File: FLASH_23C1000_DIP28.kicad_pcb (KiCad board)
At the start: 2 copper layers, 16.5 x 34.3 mm, 9 parts, among them J1 uPD23C1000, J2 Conn_1x2, J3 Conn_1x3, U1 29F010 TSOP-32 20mm, U2 29F010 sTSOP-32 14mm, U3 29F010 PLCC-32 7x9

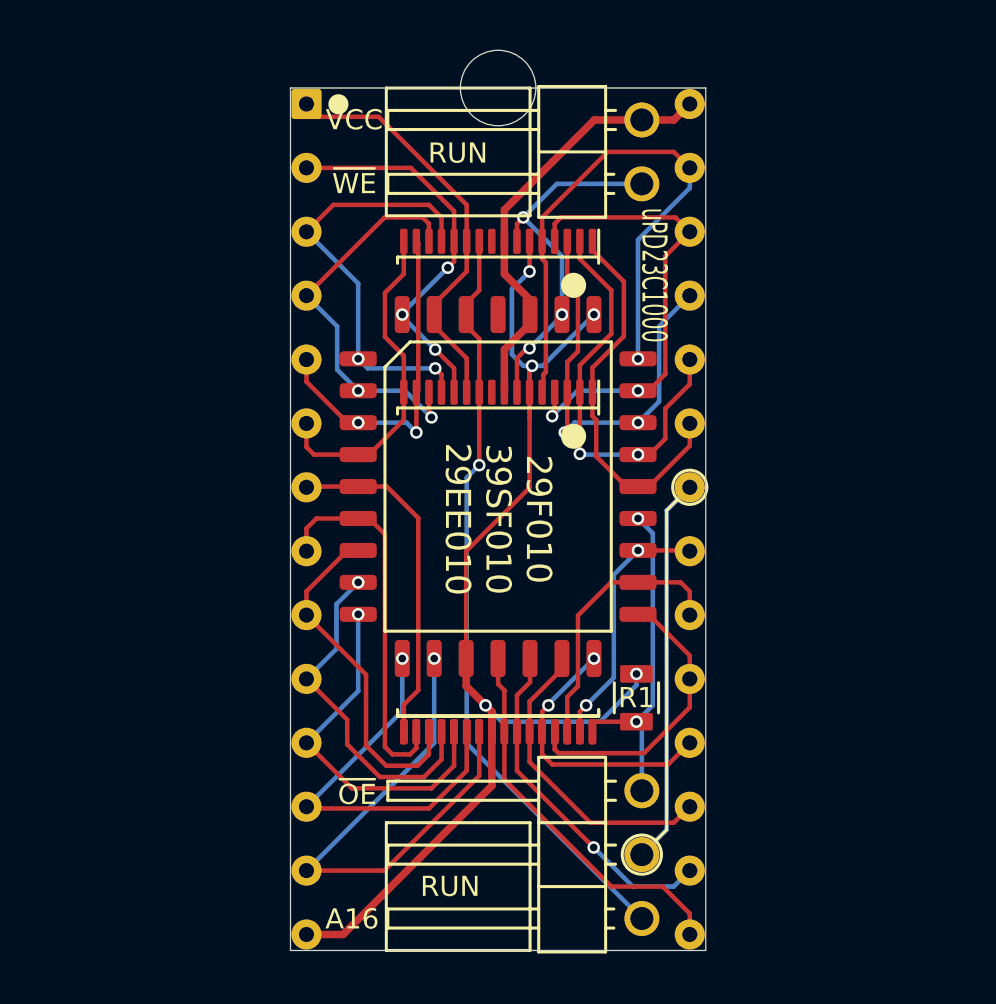
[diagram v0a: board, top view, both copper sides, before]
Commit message: Rename FlashROM_8300 to FLASH_23C1000
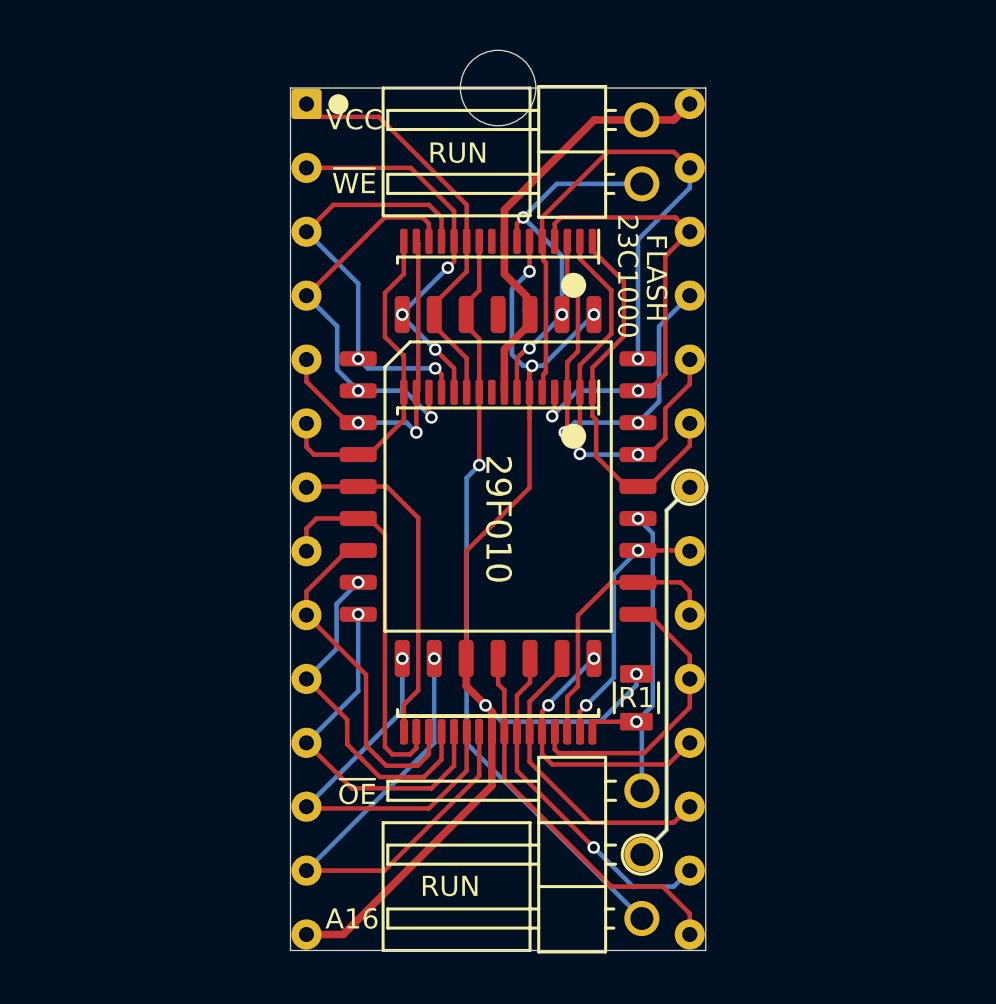
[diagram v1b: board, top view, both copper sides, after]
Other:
- board text added: "23C1000"
- board text added: "29F010"
- board text added: "29F010 to 23C1000"
- board text added: "FLASH"
- board text removed: "29F010 39SF010 29EE010"
- board text removed: "29F010 to uPD23C1000"
- board text removed: "Set programmer for installed chip (ex: SST39SF010 not uPD23C1000)"
- board text removed: "uPD23C1000"

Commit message: kicad 6
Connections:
- net /~CE renamed /~{CE}
- net /~OE renamed /~{OE}
- net /~WE renamed /~{WE}
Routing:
- net /~{CE}: track 10.9 -> 9.97 mm
- net /A17: track 11.8 -> 11.0 mm
- net /A5: track 13.7 -> 13.1 mm
- net /A4: track 13.2 -> 12.7 mm
- net /A2: track 15.0 -> 14.5 mm
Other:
- net class Default removed
- board text added: "Connect ~{WE} to programmer pin 31"
- board text added: "Move the A16 jumper to ~{OE}"
- board text added: "Remove the VCC/~{WE} jumper"
- board text added: "~{OE}"
- board text added: "~{WE}"
- board text removed: "Connect ~WE~ to programmer pin 31"
- board text removed: "Move the A16 jumper to ~OE~"
- board text removed: "Remove the VCC/~WE~ jumper"
- board text removed: "~OE"
- board text removed: "~WE"

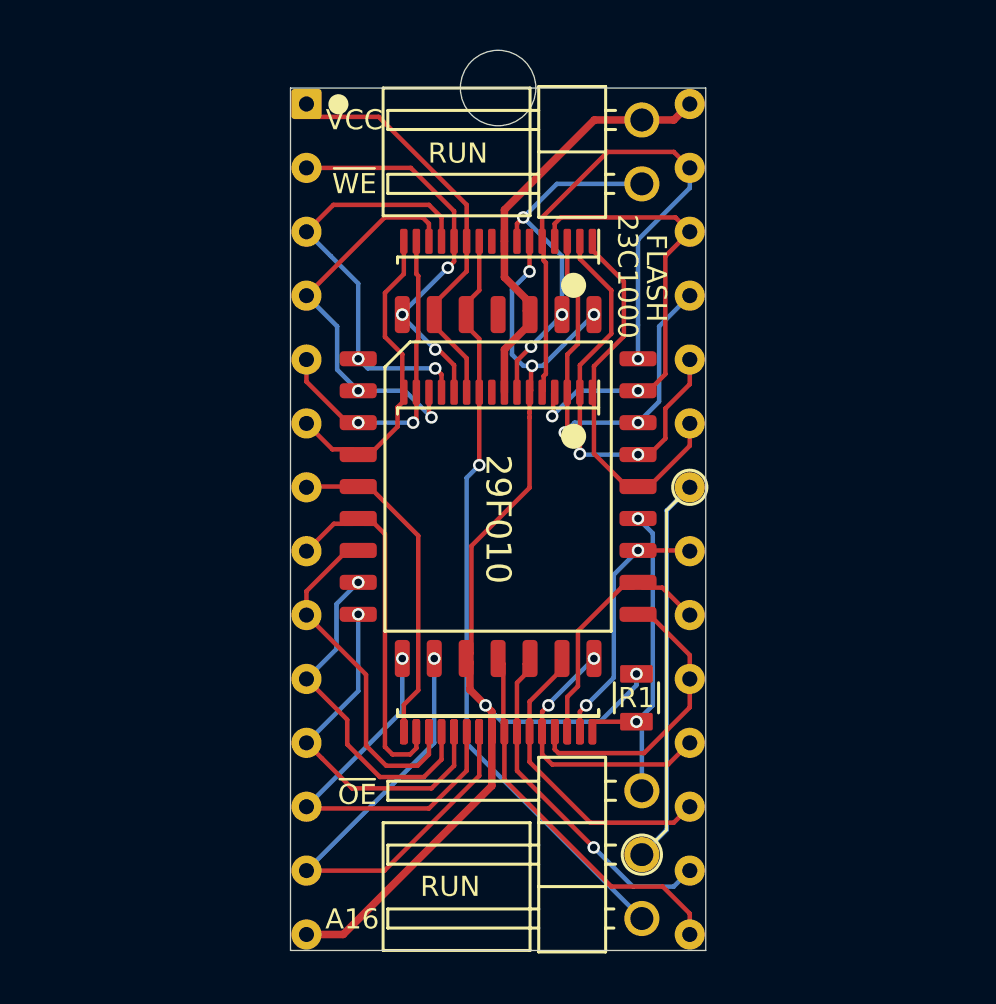
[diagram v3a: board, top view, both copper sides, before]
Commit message: Fix wrong pinout on FlashROM_100 TSOPgit add -A!
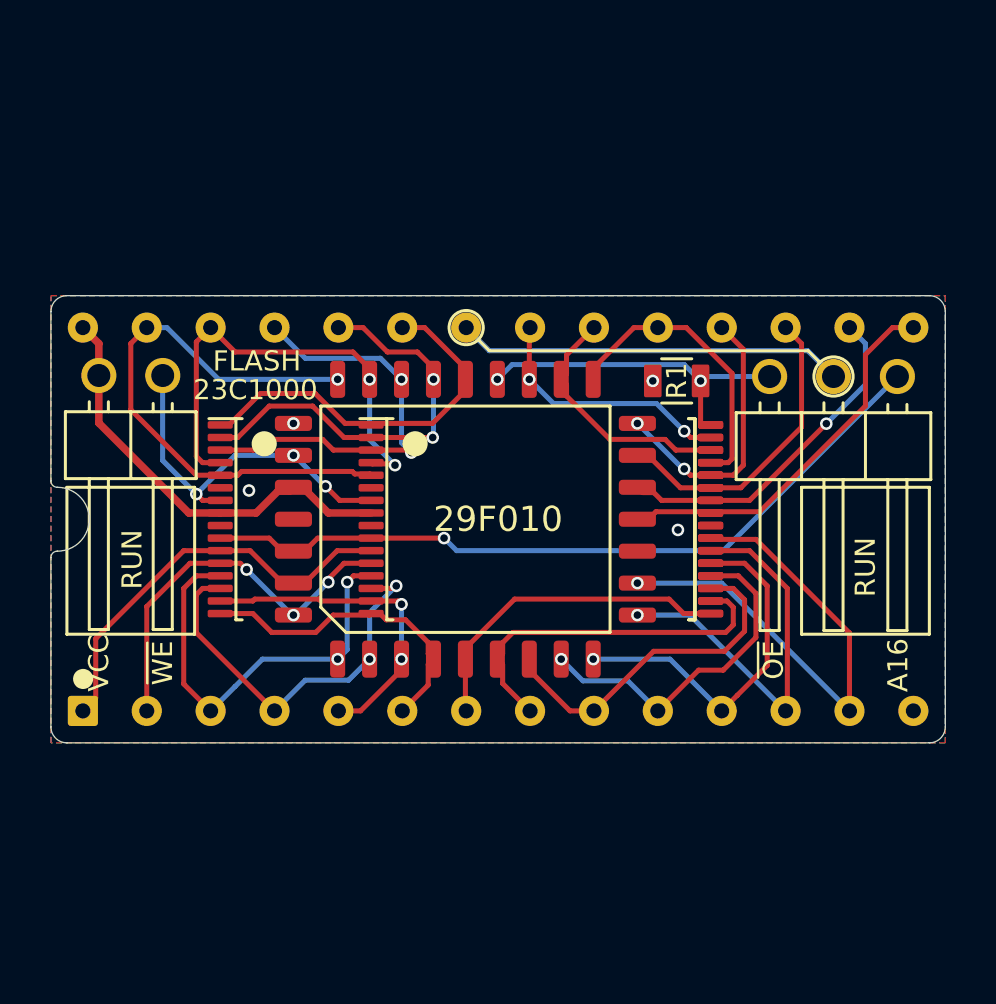
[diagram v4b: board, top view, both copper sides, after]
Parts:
- removed NT1: Net-Tie_2, 000_LOCAL:NetTie-2_SMD_0.18mm
- removed REF**: NPTH_3mm, 000_LOCAL:NPTH_3mm
- J1: value uPD23C1000 -> 23C1000
- moved J3 23.8 mm to (165.9, 93.1), turned to -90 degrees
- moved J2 20.5 mm to (136.7, 93.0), turned to -90 degrees
- moved R1 12.7 mm to (157.1, 93.2), turned to 180 degrees
- moved U2 2.40 mm to (151.7, 98.8), turned to -90 degrees
- moved U1 1.84 mm to (148.7, 98.8), turned to -90 degrees
- moved U3 1.84 mm to (148.7, 98.8), turned to 90 degrees
- turned J1 to 90 degrees
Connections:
- U1 pad 6: /A17 -> /GND
- U1 pad 9: (no net) -> unconnected-(U1-Pad9)
- U2 pad 6: /A17 -> /GND
- U2 pad 9: (no net) -> unconnected-(U2-Pad9)
- U3 pad 1: (no net) -> unconnected-(U3-Pad1)
- U3 pad 30: /A17 -> /GND
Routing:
- net /GND: track 33.3 -> 0.00 mm, vias 2 -> 4
- net /A17: track 11.0 -> 0.00 mm, vias 3 -> 0
- added copper zone on B.Cu, net /GND
- added copper zone on F.Cu, net /GND
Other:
- board size 16.5 x 34.3 mm -> 35.6 x 17.8 mm
- board text added: "${COMMENT1} ${TITLE} ${REVISION}"
- board text added: "R1: ${00000000-0000-0000-0000-00005e638d11:VALUE} Legs: TE 1544210"
- board text added: "To program: Place board in programmer, 2 rows from the top Move the A16 jumper to ~{OE} Connect A16 to programmer pin 2 Remove the VCC/~{WE} jumper Connect ~{WE} to programmer pin 31 Connect VCC to programmer pin 32"
- board text removed: "Connect A16 to programmer pin 2"
- board text removed: "Connect VCC to programmer pin 32"
- board text removed: "Connect ~{WE} to programmer pin 31"
- board text removed: "Legs: TE 1544210"
- board text removed: "Move the A16 jumper to ~{OE}"
- board text removed: "Place board in programmer, 2 rows from the top"
- board text removed: "R1: 47k"
- board text removed: "Remove the VCC/~{WE} jumper"
- board text removed: "To program the flash chip:"
- board text removed: "github.com/bkw777/aDIPters"

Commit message: 23C100 DIP28 outline, gnd, silk
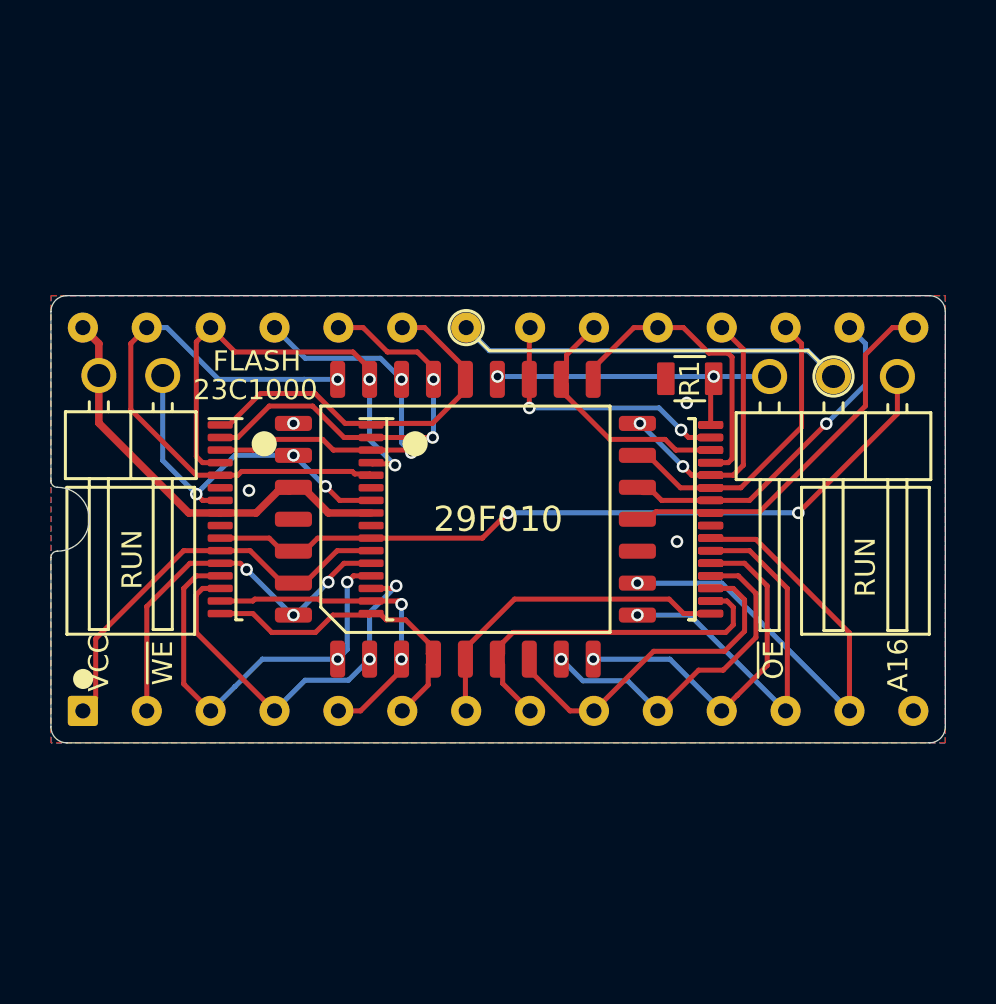
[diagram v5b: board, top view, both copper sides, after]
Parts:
- moved R1 0.53 mm to (157.6, 93.2)
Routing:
- net /~{OE}: track 13.5 -> 12.8 mm
- net /A10: track 10.2 -> 10.9 mm
- net /A16: track 30.4 -> 30.9 mm, vias 1 -> 2
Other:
- board text added: "RUN: Jumper labeled RUN positions. Install board in place of 23C1000. PROGRAM: Place board in programmer, board pin 1 in programmer pin 3. Remove VCC/~{WE} jumper. Move A16 jumper to ~{OE}. Connect A16 to programmer pin 2, ~{WE} to programmer pin 31, VCC to programmer pin 32. Program as 29F010."
- board text removed: "To program: Place board in programmer, 2 rows from the top Move the A16 jumper to ~{OE} Connect A16 to programmer pin 2 Remove the VCC/~{WE} jumper Connect ~{WE} to programmer pin 31 Connect VCC to programmer pin 32"

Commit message: dual tsop footprint on flash_23c100_dip28
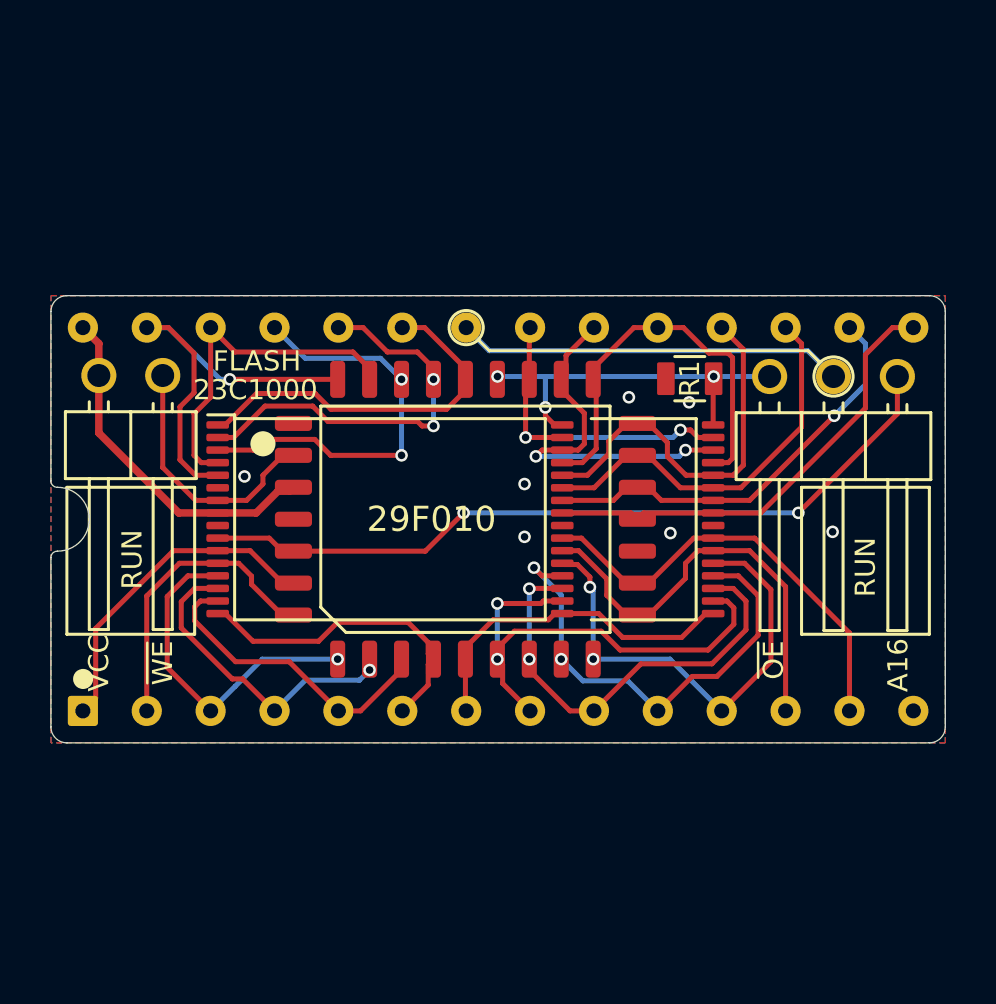
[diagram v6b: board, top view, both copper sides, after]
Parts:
- removed the U2 at (151.7, 98.8)
- U1: value 29F010 TSOP-32 20mm -> 29F010 TSOP-32; footprint 000_LOCAL:TSOP32-20mm -> 000_LOCAL:TSOP32-dual
- turned U1 to 0 degrees
- renumbered U3 to U2
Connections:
- net /GND renamed GND
- net /VCC renamed VCC
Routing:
- net /A14: track 22.7 -> 17.0 mm
- net /A2: track 14.5 -> 19.9 mm, vias 0 -> 2
- net /A0: track 13.6 -> 19.0 mm, vias 1 -> 2
- net /~{CE}: track 9.97 -> 14.8 mm, vias 0 -> 2
- net /A13: track 18.7 -> 13.8 mm, vias 2 -> 0
- net /D0: track 14.3 -> 19.0 mm, vias 1 -> 2
- net /D6: track 11.1 -> 15.6 mm, vias 2 -> 0
- net /D7: track 12.1 -> 16.4 mm
- net /~{WE}: track 14.7 -> 10.3 mm, vias 3 -> 0
- net /A1: track 13.8 -> 17.8 mm, vias 0 -> 2
- net /A7: track 17.1 -> 13.5 mm, vias 2 -> 1
- net /A12: track 15.6 -> 12.0 mm, vias 3 -> 0
- net /D5: track 11.9 -> 15.4 mm
- net /A15: track 16.5 -> 13.2 mm
- net /A6: track 16.0 -> 12.7 mm, vias 2 -> 1
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
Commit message: 23C1000 DIP-28 tsop-32 daul footprint & teardrops
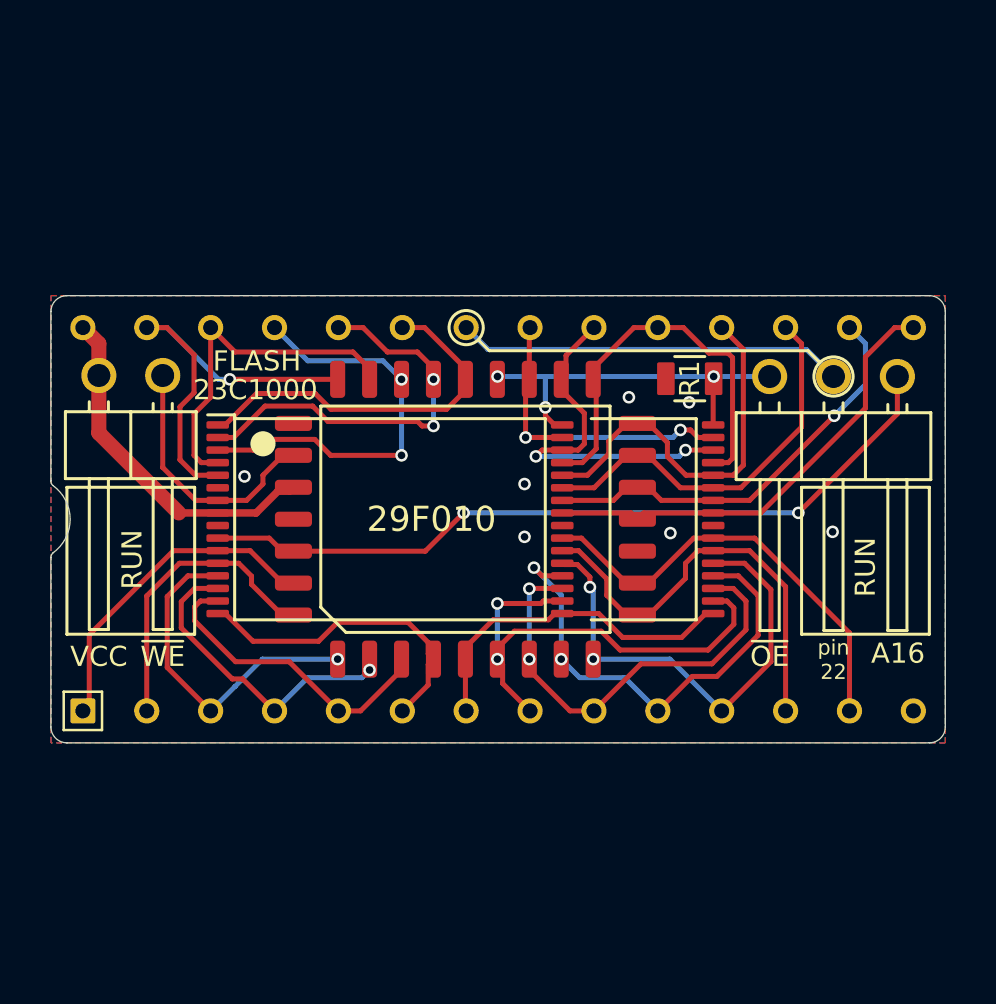
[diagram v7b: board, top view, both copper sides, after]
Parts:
- J1: footprint 000_LOCAL:DIP28_0.6_pcb_sil_pins -> 000_LOCAL:DIP-28_600_pcb_shallow_notch
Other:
- outline, holes or cut-outs redrawn
- board text added: "TO PROGRAM: Place board offset with board pin 1 in programmer pin 3. Move A16 jumper to ~{OE}. Connect A16 to programmer pin 2. Remove VCC/~{WE} jumper. Connect ~{WE} to programmer pin 31. Connect VCC to programmer pin 32. Program as 29F010. TO RUN (emulate a 23C1000): Both jumpers on RUN positions. Install board in place of 23C1000."
- board text added: "pin 22"
- board text removed: "RUN: Jumper labeled RUN positions. Install board in place of 23C1000. PROGRAM: Place board in programmer, board pin 1 in programmer pin 3. Remove VCC/~{WE} jumper. Move A16 jumper to ~{OE}. Connect A16 to programmer pin 2, ~{WE} to programmer pin 31, VCC to programmer pin 32. Program as 29F010."
